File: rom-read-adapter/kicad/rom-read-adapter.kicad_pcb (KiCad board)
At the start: 2 copper layers, 100 x 100 mm, 27 parts

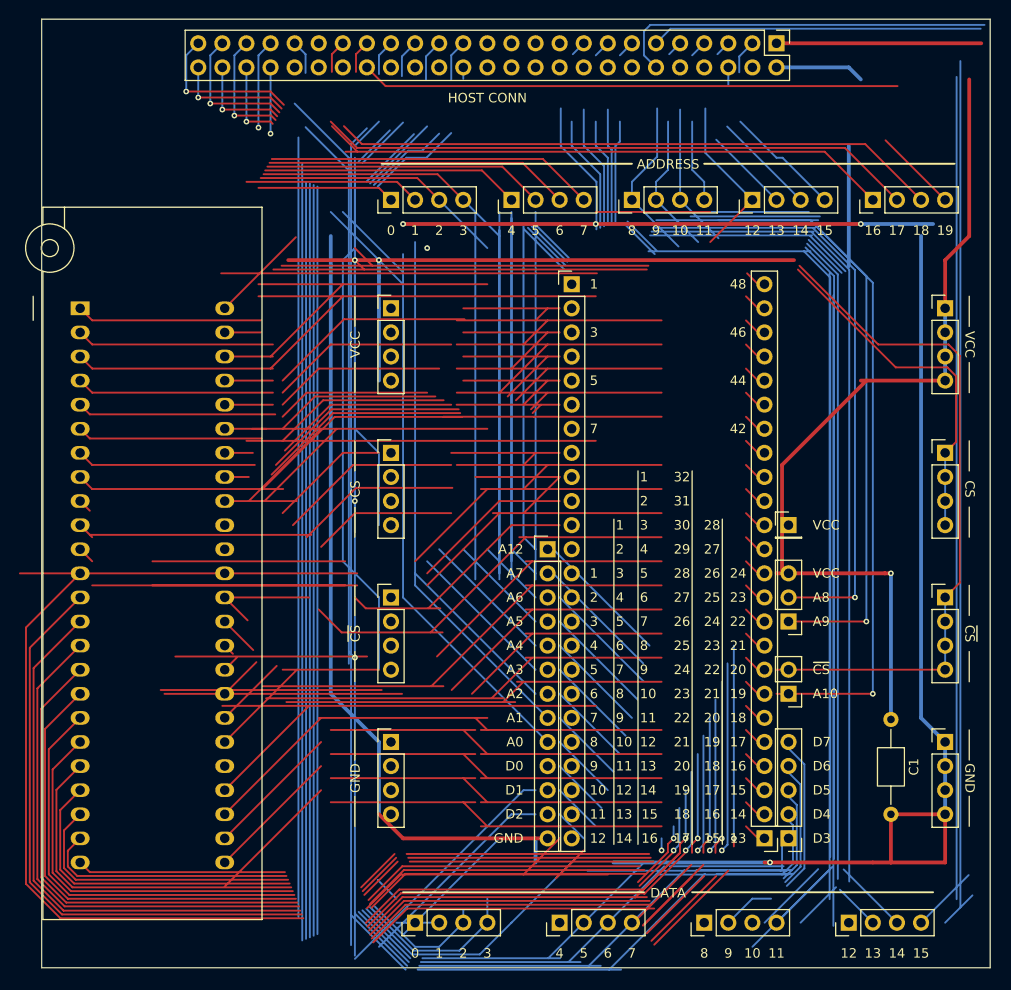
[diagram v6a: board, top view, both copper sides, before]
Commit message: WIP rom-read-adapter pcb: Added mounting holes
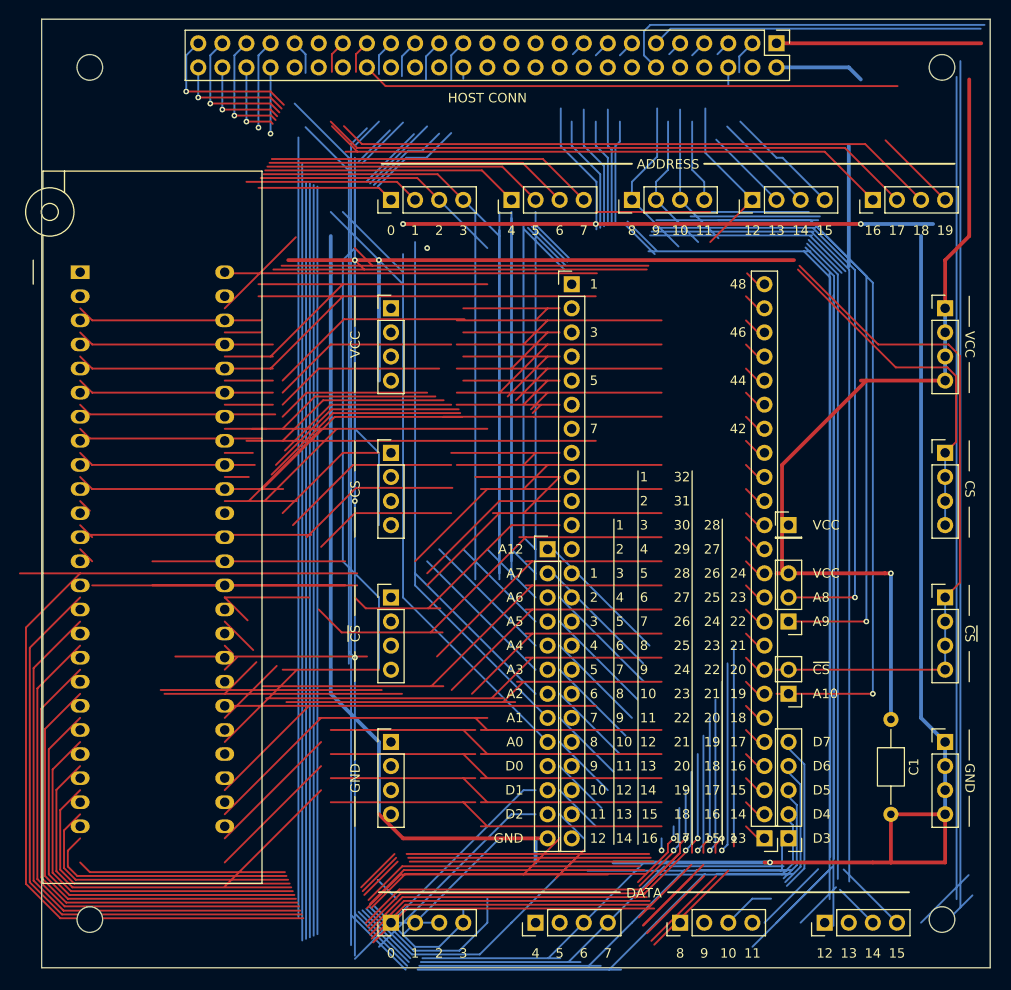
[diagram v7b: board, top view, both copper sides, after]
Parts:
- added REF**: MountingHole_2.7mm_M2.5, MountingHole:MountingHole_2.7mm_M2.5, F.Cu at (106.7, 145.7)
- added REF**: MountingHole_2.7mm_M2.5, MountingHole:MountingHole_2.7mm_M2.5, F.Cu at (106.7, 55.9)
- added REF**: MountingHole_2.7mm_M2.5, MountingHole:MountingHole_2.7mm_M2.5, F.Cu at (196.5, 145.7)
- added REF**: MountingHole_2.7mm_M2.5, MountingHole:MountingHole_2.7mm_M2.5, F.Cu at (196.5, 55.9)
- moved JR1 3.81 mm to (105.7, 77.5)
- moved JH22 2.54 mm to (153.7, 146.1)
- moved JH21 2.54 mm to (138.4, 146.1)
- moved JH23 2.54 mm to (168.9, 146.1)
- moved JH24 2.54 mm to (184.2, 146.1)
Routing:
- net D12: track 24.1 -> 338.3 mm
- net D11: track 372.6 -> 58.5 mm
- net Net-(JR1-Pin_12): track 101.4 -> 35.5 mm
- net Net-(JR1-Pin_13): track 166.4 -> 105.9 mm
- net Net-(JR1-Pin_27): track 92.7 -> 39.7 mm
- net Net-(JR1-Pin_11): track 77.0 -> 28.4 mm
- net Net-(JR1-Pin_20): track 44.8 -> 89.4 mm
- net Net-(JR1-Pin_35): track 54.4 -> 98.4 mm
- net Net-(JR1-Pin_14): track 136.9 -> 179.5 mm
- net Net-(JR1-Pin_21): track 40.3 -> 81.4 mm
- net Net-(JR1-Pin_26): track 54.0 -> 92.7 mm
- net Net-(JR1-Pin_38): track 37.3 -> 1.79 mm
- net D7: track 390.2 -> 369.5 mm
- net D8: track 1.63 -> 22.4 mm
- net Net-(JR1-Pin_39): track 22.1 -> 1.79 mm
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
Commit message: WIP rom-read-adapter pcb: Re-routing
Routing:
- net D12: track 338.3 -> 117.8 mm
- net A12: track 143.3 -> 18.6 mm, vias 3 -> 0
- net D8: track 22.4 -> 146.8 mm
- net D15: track 227.6 -> 115.0 mm, vias 0 -> 2
- net A10: track 101.2 -> 17.6 mm, vias 1 -> 0
- net D14: track 39.8 -> 118.8 mm
- net D9: track 48.3 -> 121.4 mm
- net A8: track 81.3 -> 18.6 mm, vias 1 -> 0
- net D11: track 58.5 -> 118.6 mm
- net A9: track 68.1 -> 15.0 mm, vias 1 -> 0
- net D10: track 98.0 -> 122.5 mm
- net GND: track 418.9 -> 438.1 mm
- net A2: track 71.7 -> 87.4 mm
- net unconnected-(JH1-P20-Pad20): track 12.1 -> 0.00 mm
- net A1: track 101.9 -> 91.5 mm
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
